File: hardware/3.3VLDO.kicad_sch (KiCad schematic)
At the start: 5 parts, among them U11 MCP1826S

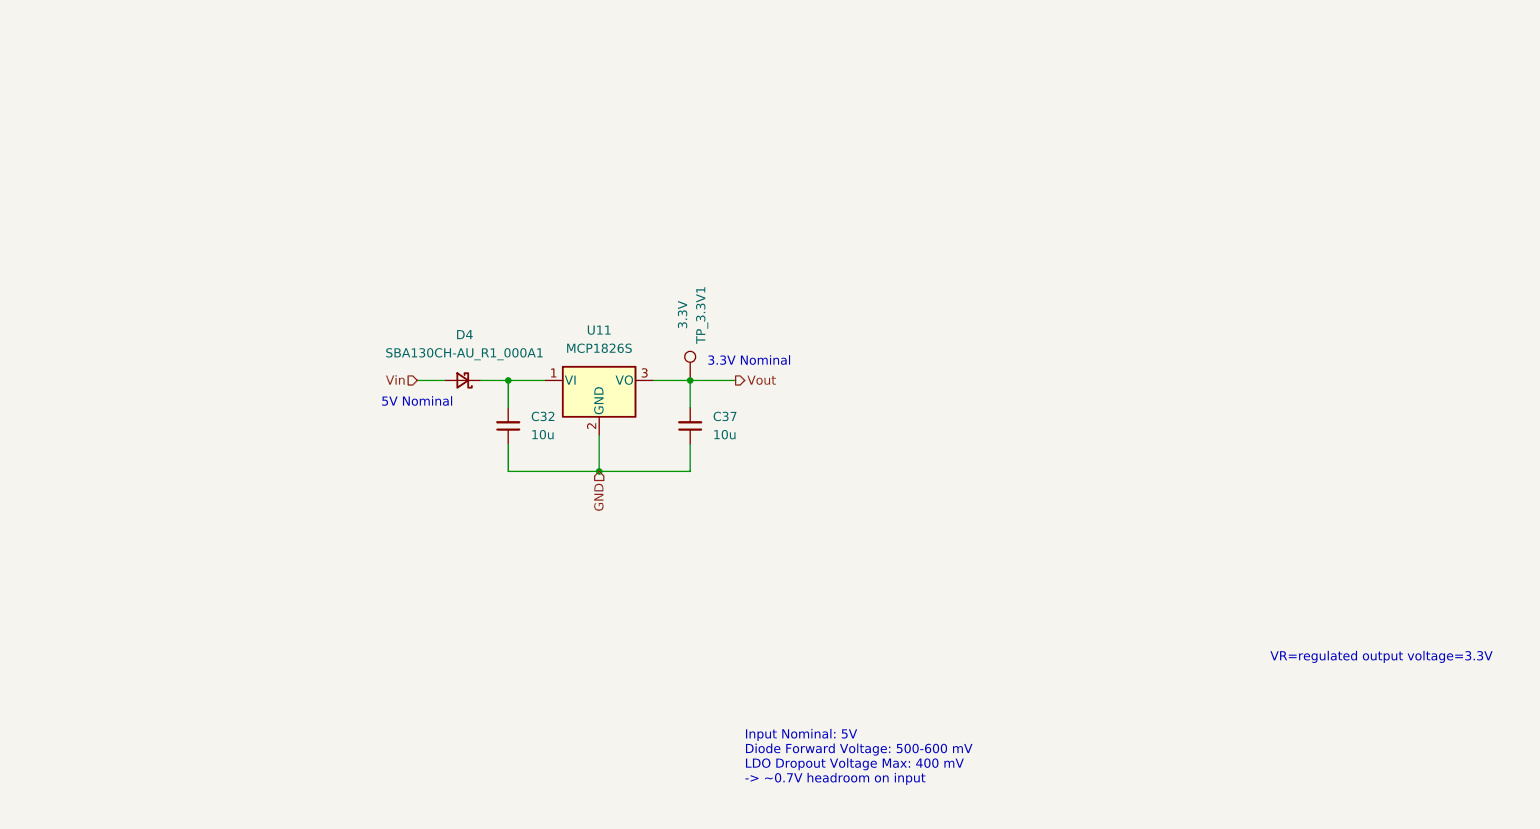
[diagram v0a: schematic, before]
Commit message: nearly all reviews addressed yippeeeeee
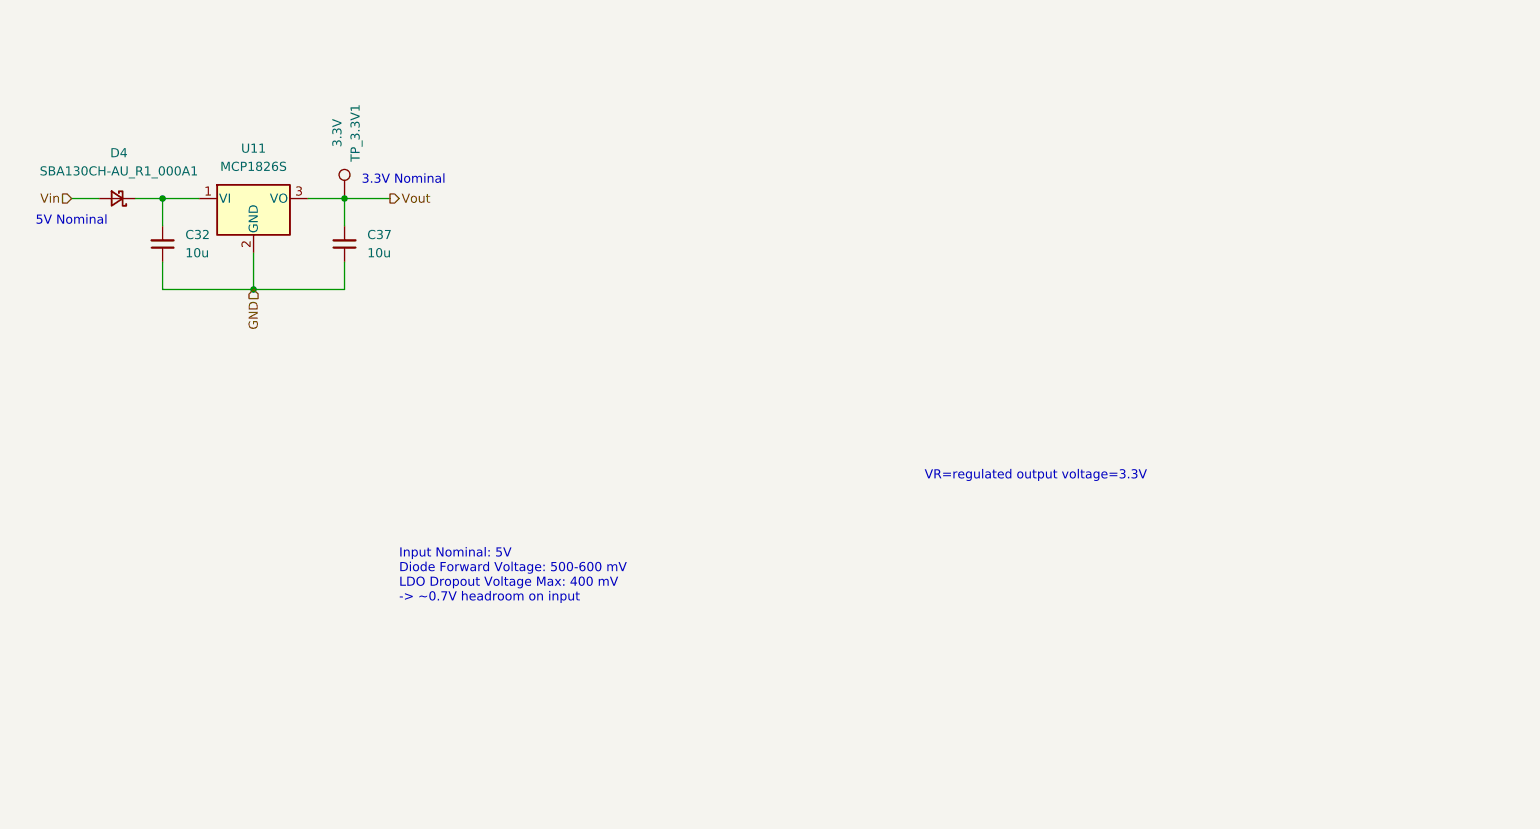
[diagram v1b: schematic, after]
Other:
- moved on the sheet: C32, C37, D4, TP_3.3V1, U11

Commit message: done all obbb specific reviews beside indicator led resistor values + math, goodnight
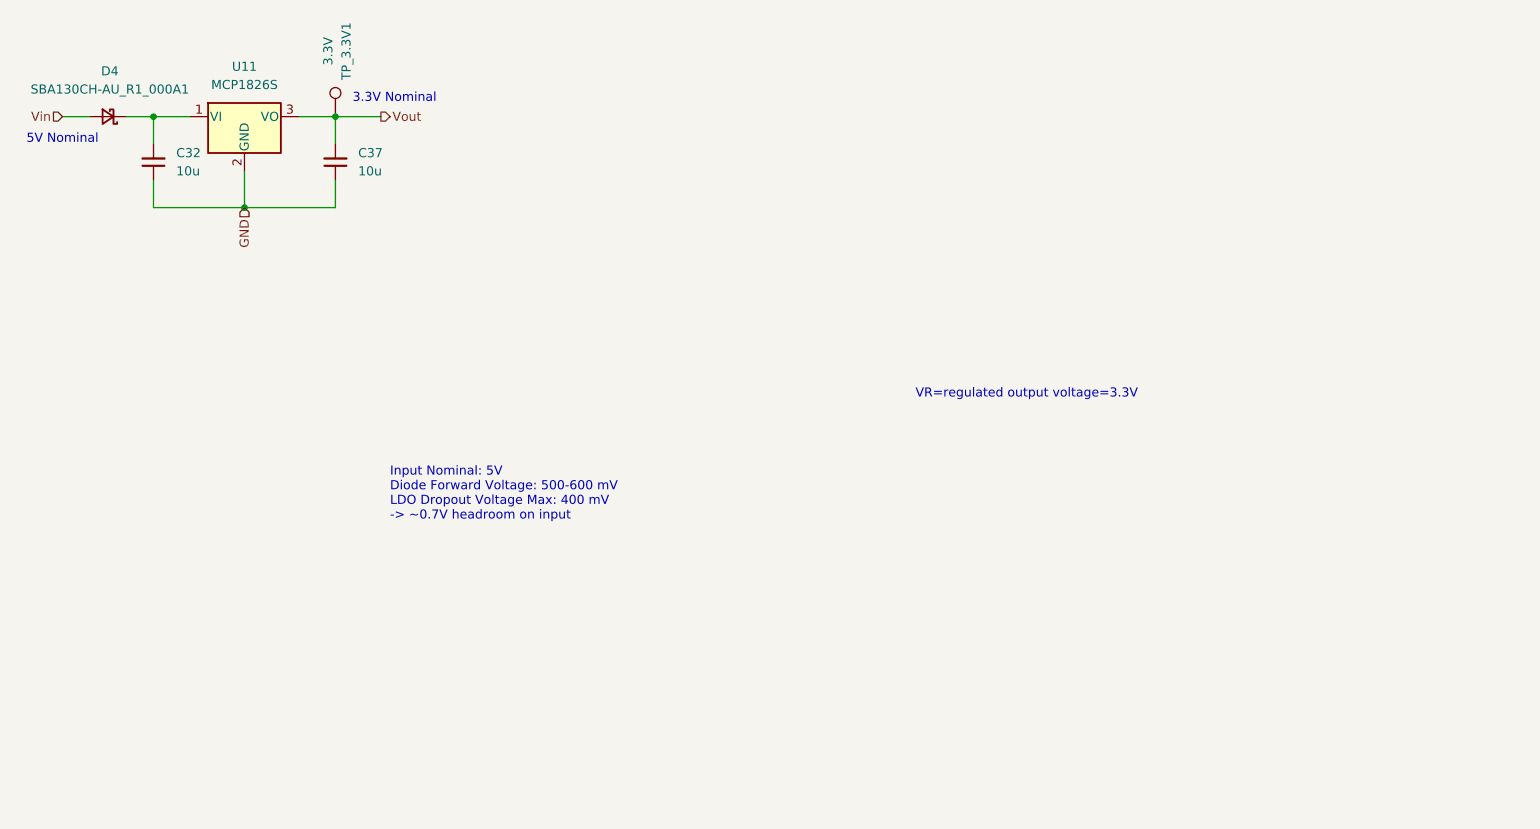
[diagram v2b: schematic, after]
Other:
- moved on the sheet: C32, C37, D4, TP_3.3V1, U11

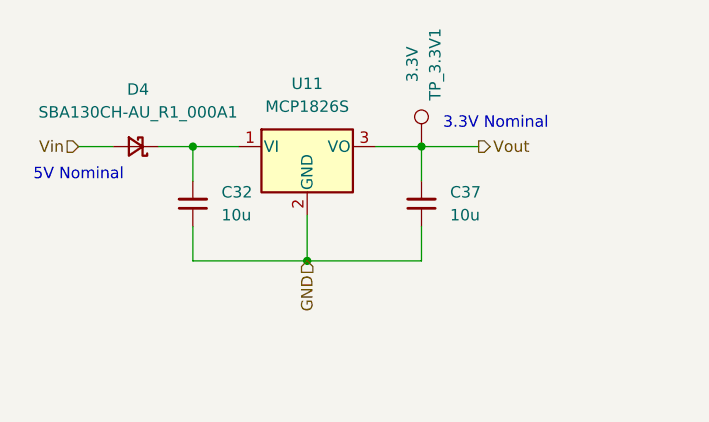
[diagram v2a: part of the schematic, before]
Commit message: fixes only thing left is finish assigning footprints, its frozen
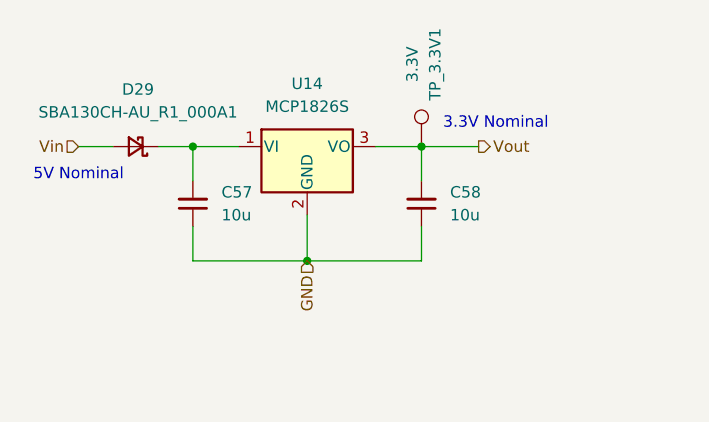
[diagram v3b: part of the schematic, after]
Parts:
- renumbered C32 to C57, C37 to C58, D4 to D29, U11 to U14
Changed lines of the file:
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@@
 		(dnp no)
 		(fields_autoplaced yes)
-		(property "Reference" "C37"
+		(property "Reference" "C58"
 			(at 74.295 50.7935 0)
 			(show_name no)
@@
 			(project "PS-LVCarrier"
 				(path "/9bab2d9d-20f3-40ef-8545-e1299efec47e/194a8848-c0d2-44dd-9e5b-1946509490d6/c6cd08f1-d43d-47b8-96e3-b45d3e433ee3"
-					(reference "C37")
+					(reference "C58")
 					(unit 1)
 				)
@@
 		(dnp no)
 		(fields_autoplaced yes)
-		(property "Reference" "U11"
+		(property "Reference" "U14"
 			(at 58.42 38.735 0)
 			(show_name no)
@@
 			(project "PS-LVCarrier"
 				(path "/9bab2d9d-20f3-40ef-8545-e1299efec47e/194a8848-c0d2-44dd-9e5b-1946509490d6/c6cd08f1-d43d-47b8-96e3-b45d3e433ee3"
-					(reference "U11")
+					(reference "U14")
 					(unit 1)
 				)
@@
 		(dnp no)
 		(fields_autoplaced yes)
-		(property "Reference" "D4"
+		(property "Reference" "D29"
 			(at 39.624 39.37 0)
 			(show_name no)
@@
 			(project "PS-LVCarrier"
 				(path "/9bab2d9d-20f3-40ef-8545-e1299efec47e/194a8848-c0d2-44dd-9e5b-1946509490d6/c6cd08f1-d43d-47b8-96e3-b45d3e433ee3"
-					(reference "D4")
+					(reference "D29")
 					(unit 1)
 				)
@@
 		(dnp no)
 		(fields_autoplaced yes)
-		(property "Reference" "C32"
+		(property "Reference" "C57"
 			(at 48.895 50.7935 0)
 			(show_name no)
@@
 			(project "PS-LVCarrier"
 				(path "/9bab2d9d-20f3-40ef-8545-e1299efec47e/194a8848-c0d2-44dd-9e5b-1946509490d6/c6cd08f1-d43d-47b8-96e3-b45d3e433ee3"
-					(reference "C32")
-					(unit 1)
-				)
+					(reference "C57")
+					(unit 1)
+				)

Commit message: breh
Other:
- moved on the sheet: C57, C58, D29, TP_3.3V1, U14

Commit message: switch branch
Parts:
- renumbered C57 to C65, C58 to C66
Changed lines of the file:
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@@
 		(dnp no)
 		(fields_autoplaced yes)
-		(property "Reference" "C58"
+		(property "Reference" "C66"
 			(at 78.105 64.7635 0)
 			(show_name no)
@@
 			(project "PS-LVCarrier"
 				(path "/9bab2d9d-20f3-40ef-8545-e1299efec47e/194a8848-c0d2-44dd-9e5b-1946509490d6/c6cd08f1-d43d-47b8-96e3-b45d3e433ee3"
-					(reference "C58")
+					(reference "C66")
 					(unit 1)
 				)
@@
 		(dnp no)
 		(fields_autoplaced yes)
-		(property "Reference" "C57"
+		(property "Reference" "C65"
 			(at 52.705 64.7635 0)
 			(show_name no)
@@
 			(project "PS-LVCarrier"
 				(path "/9bab2d9d-20f3-40ef-8545-e1299efec47e/194a8848-c0d2-44dd-9e5b-1946509490d6/c6cd08f1-d43d-47b8-96e3-b45d3e433ee3"
-					(reference "C57")
-					(unit 1)
-				)
+					(reference "C65")
+					(unit 1)
+				)

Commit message: review ts
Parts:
- renumbered C65 to C51, C66 to C52, D29 to D18, U14 to U11
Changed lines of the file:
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@@
 		(dnp no)
 		(fields_autoplaced yes)
-		(property "Reference" "C66"
+		(property "Reference" "C52"
 			(at 78.105 64.7635 0)
 			(show_name no)
@@
 			(project "PS-LVCarrier"
 				(path "/9bab2d9d-20f3-40ef-8545-e1299efec47e/194a8848-c0d2-44dd-9e5b-1946509490d6/c6cd08f1-d43d-47b8-96e3-b45d3e433ee3"
-					(reference "C66")
+					(reference "C52")
 					(unit 1)
 				)
@@
 		(dnp no)
 		(fields_autoplaced yes)
-		(property "Reference" "U14"
+		(property "Reference" "U11"
 			(at 62.23 52.705 0)
 			(show_name no)
@@
 			(project "PS-LVCarrier"
 				(path "/9bab2d9d-20f3-40ef-8545-e1299efec47e/194a8848-c0d2-44dd-9e5b-1946509490d6/c6cd08f1-d43d-47b8-96e3-b45d3e433ee3"
-					(reference "U14")
+					(reference "U11")
 					(unit 1)
 				)
@@
 		(dnp no)
 		(fields_autoplaced yes)
-		(property "Reference" "D29"
+		(property "Reference" "D18"
 			(at 43.434 53.34 0)
 			(show_name no)
@@
 			(project "PS-LVCarrier"
 				(path "/9bab2d9d-20f3-40ef-8545-e1299efec47e/194a8848-c0d2-44dd-9e5b-1946509490d6/c6cd08f1-d43d-47b8-96e3-b45d3e433ee3"
-					(reference "D29")
+					(reference "D18")
 					(unit 1)
 				)
@@
 		(dnp no)
 		(fields_autoplaced yes)
-		(property "Reference" "C65"
+		(property "Reference" "C51"
 			(at 52.705 64.7635 0)
 			(show_name no)
@@
 			(project "PS-LVCarrier"
 				(path "/9bab2d9d-20f3-40ef-8545-e1299efec47e/194a8848-c0d2-44dd-9e5b-1946509490d6/c6cd08f1-d43d-47b8-96e3-b45d3e433ee3"
-					(reference "C65")
-					(unit 1)
-				)
+					(reference "C51")
+					(unit 1)
+				)

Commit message: addressed
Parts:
- removed D18: SBA130CH-AU_R1_000A1, Diode_SMD:D_SOD-323_HandSoldering, symbol Device:D_Schottky_Small
- removed TP_3.3V1: 3.3V, TestPoint:TestPoint_Loop_D1.80mm_Drill1.0mm_Beaded, symbol Connector:TestPoint
- removed U11: MCP1826S, Package_TO_SOT_SMD:SOT-223-3_TabPin2, symbol Regulator_Linear:MCP1826S
- added D24: SBA130CH-AU_R1_000A1, Diode_SMD:D_SOD-323_HandSoldering, symbol Device:D_Schottky_Small
- added TP_3.3V2: 3.3V, TestPoint:TestPoint_Loop_D1.80mm_Drill1.0mm_Beaded, symbol Connector:TestPoint
- added U14: MCP1826S, Package_TO_SOT_SMD:SOT-223-3_TabPin2, symbol Regulator_Linear:MCP1826S
- renumbered C51 to C76, C52 to C77
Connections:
- net GND: now also U14.2 (GND)
- net Vin: now also D24.2 (A)
- net Vout: now also TP_3.3V2.1, U14.3 (VO)
- net at C76.2: now also D24.1 (K), U14.1 (VI)
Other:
- moved on the sheet: C76, C77
